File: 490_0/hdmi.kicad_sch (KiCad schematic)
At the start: 8 parts, among them J28 HDMI_D_1.4, U10 EMI8142MUTAG, U11 EMI8142MUTAG

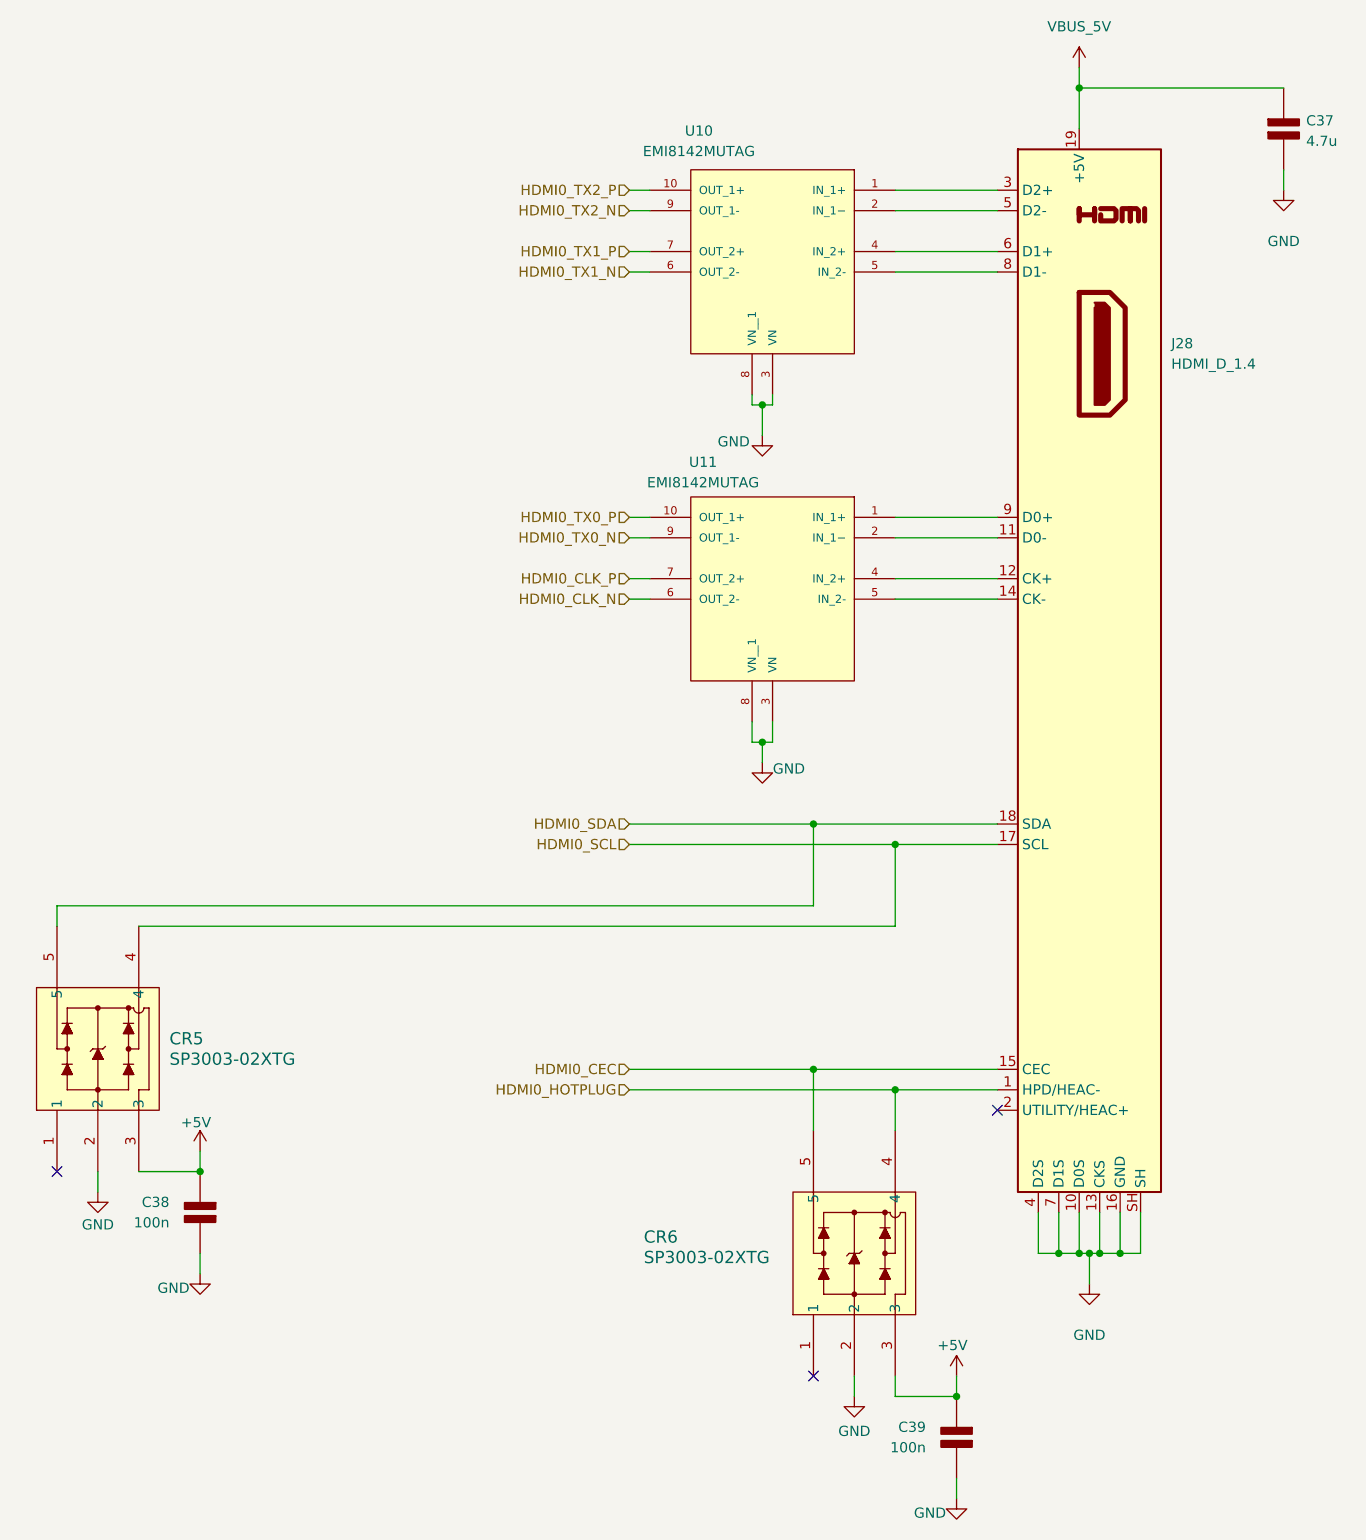
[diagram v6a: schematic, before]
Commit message: Power + BOM update
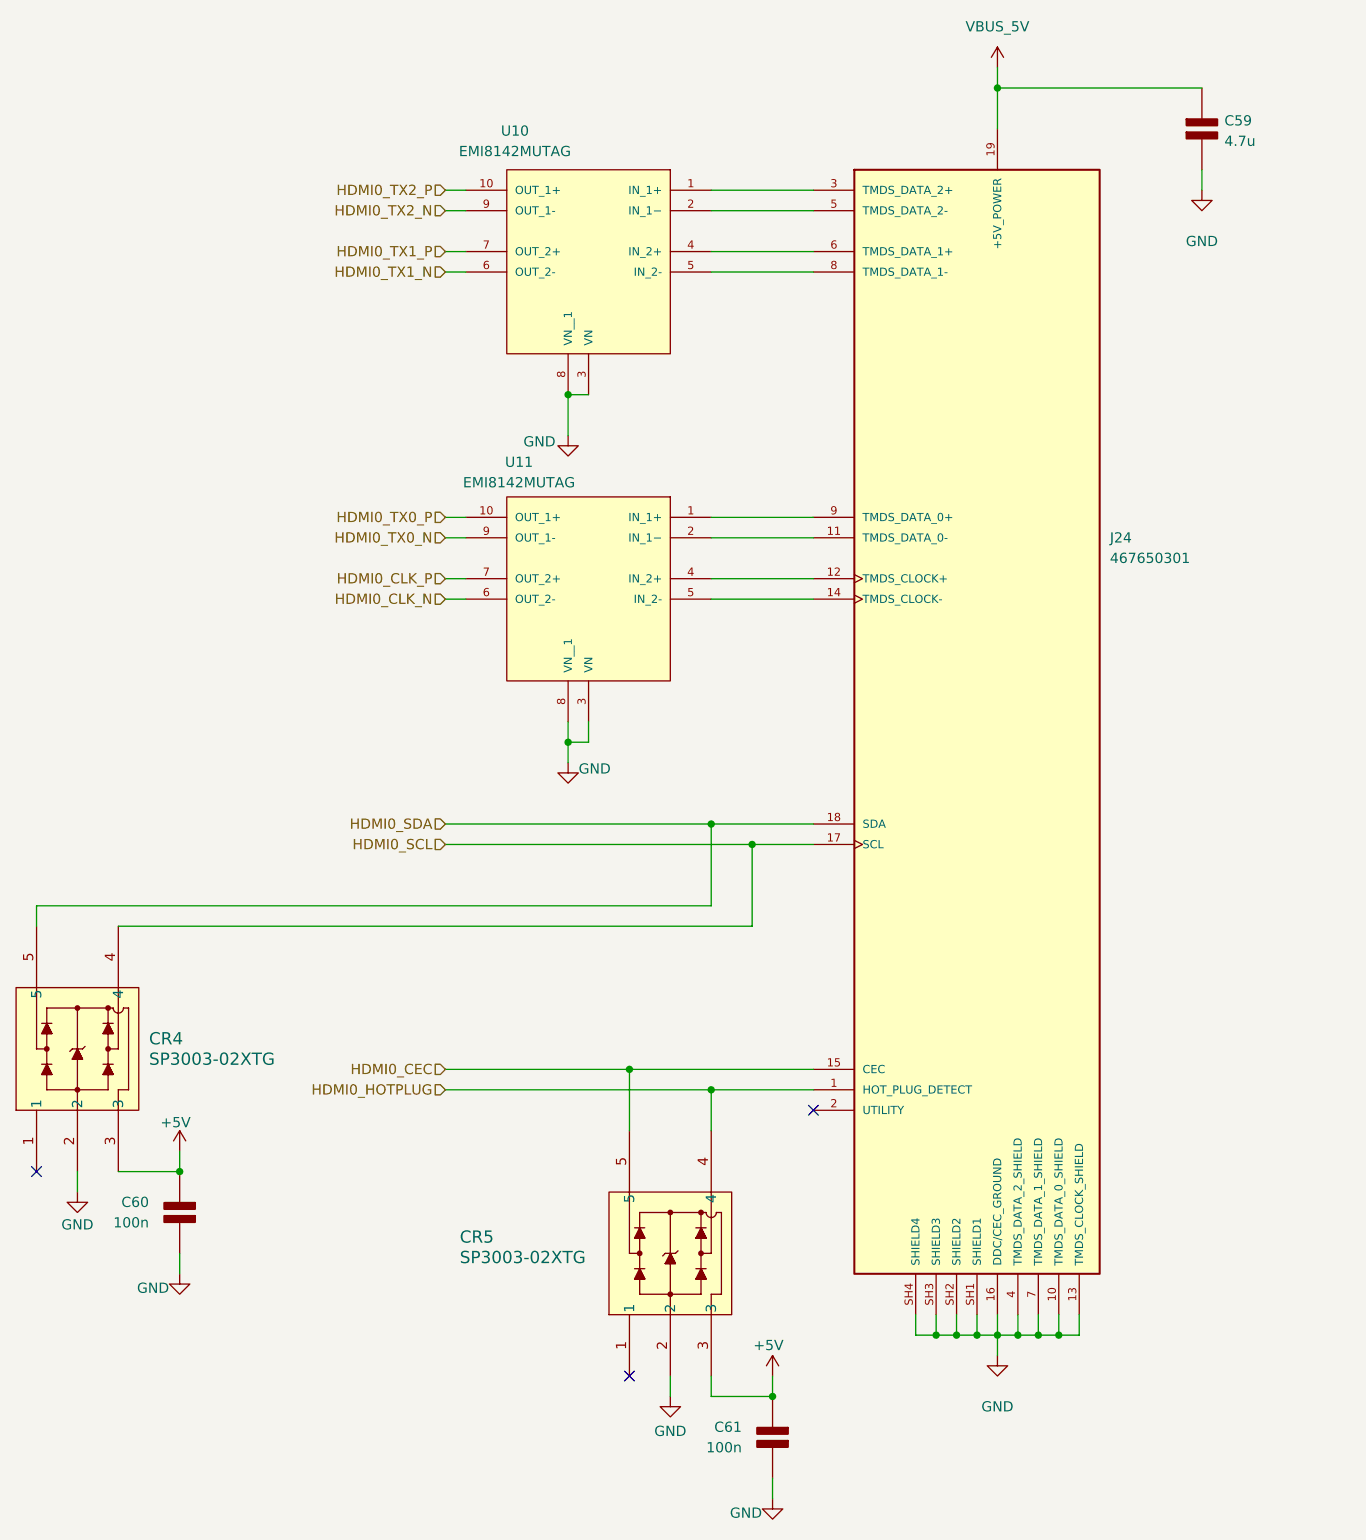
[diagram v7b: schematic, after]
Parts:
- removed J28: HDMI_D_1.4, symbol Connector:HDMI_D_1.4
- added J24: 467650301, 467650301:MOLEX_467650301, symbol capstone_parts:467650301
- CR4: renamed from CR5; footprint SOT553_LTF -> (none)
- CR5: renamed from CR6; footprint SOT553_LTF -> (none)
- U11: footprint EMI8142MUTAG:SON40P220X135X50-10N -> (none)
- renumbered C37 to C59, C38 to C60, C39 to C61
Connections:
- net GND: now also J24.10 (TMDS_DATA_0_SHIELD), J24.13 (TMDS_CLOCK_SHIELD), J24.16 (DDC/CEC_GROUND), J24.4 (TMDS_DATA_2_SHIELD), J24.7 (TMDS_DATA_1_SHIELD), J24.SH1 (SHIELD1), J24.SH2 (SHIELD2), J24.SH3 (SHIELD3), J24.SH4 (SHIELD4)
- net HDMI0_CEC: now also J24.15 (CEC)
- net HDMI0_HOTPLUG: now also J24.1 (HOT_PLUG_DETECT)
- net HDMI0_SCL: now also J24.17 (SCL)
- net HDMI0_SDA: now also J24.18 (SDA)
- net VBUS_5V: now also J24.19 (+5V_POWER)
- net at U11.2 (IN_1−): now also J24.11 (TMDS_DATA_0-)
- net at U11.4 (IN_2+): now also J24.12 (TMDS_CLOCK+)
- net at U11.5 (IN_2-): now also J24.14 (TMDS_CLOCK-)
- net at U10.1 (IN_1+): now also J24.3 (TMDS_DATA_2+)
- net at U10.2 (IN_1−): now also J24.5 (TMDS_DATA_2-)
- net at U10.4 (IN_2+): now also J24.6 (TMDS_DATA_1+)
- net at U10.5 (IN_2-): now also J24.8 (TMDS_DATA_1-)
- net at U11.1 (IN_1+): now also J24.9 (TMDS_DATA_0+)
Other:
- moved on the sheet: C59, C60, C61, CR4, CR5, U10, U11

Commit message: finished BOM
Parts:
- C59: Digikey Link (none) -> https://www.digikey.ca/en/products/detail/kemet/c1206c475k8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; Manufacturer (none) -> KEMET; Manufacturer Part (none) -> C1206C475K8RACTU; Package (none) -> 1206 (3216 Metric); Price (none) -> 0.51; Supplier (none) -> DigiKey; Supplier P/N (none) -> 399-C1206C475K8RACTUCT-ND; Type (none) -> SMD; Unit (none) -> pcs
- C60, C61: Digikey Link (none) -> https://www.digikey.ca/en/products/detail/samsung-electro-m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; Manufacturer (none) -> Samsung Electro-Mechanics; Manufacturer Part (none) -> CL31B104KBCNNNC; Package (none) -> 1206 (3216 Metric); Price (none) -> 0.11; Supplier (none) -> DigiKey; Supplier P/N (none) -> 1276-1017-1-ND; Type (none) -> SMD, MLCC; Unit (none) -> pcs
